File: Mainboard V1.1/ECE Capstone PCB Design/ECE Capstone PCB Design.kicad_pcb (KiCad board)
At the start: 2 copper layers, 81.9 x 68.9 mm, 71 parts, among them J1 1053131105, J2 1053131105, J3 Conn_01x40_Socket, J6 60S019P-301N-B1-FEC, U1 MCP2518FDT-H/SL, U2 MCP2542FD-E/SN, U5 TPS562201, U6 TPS61165DBV, U7 TPS562201

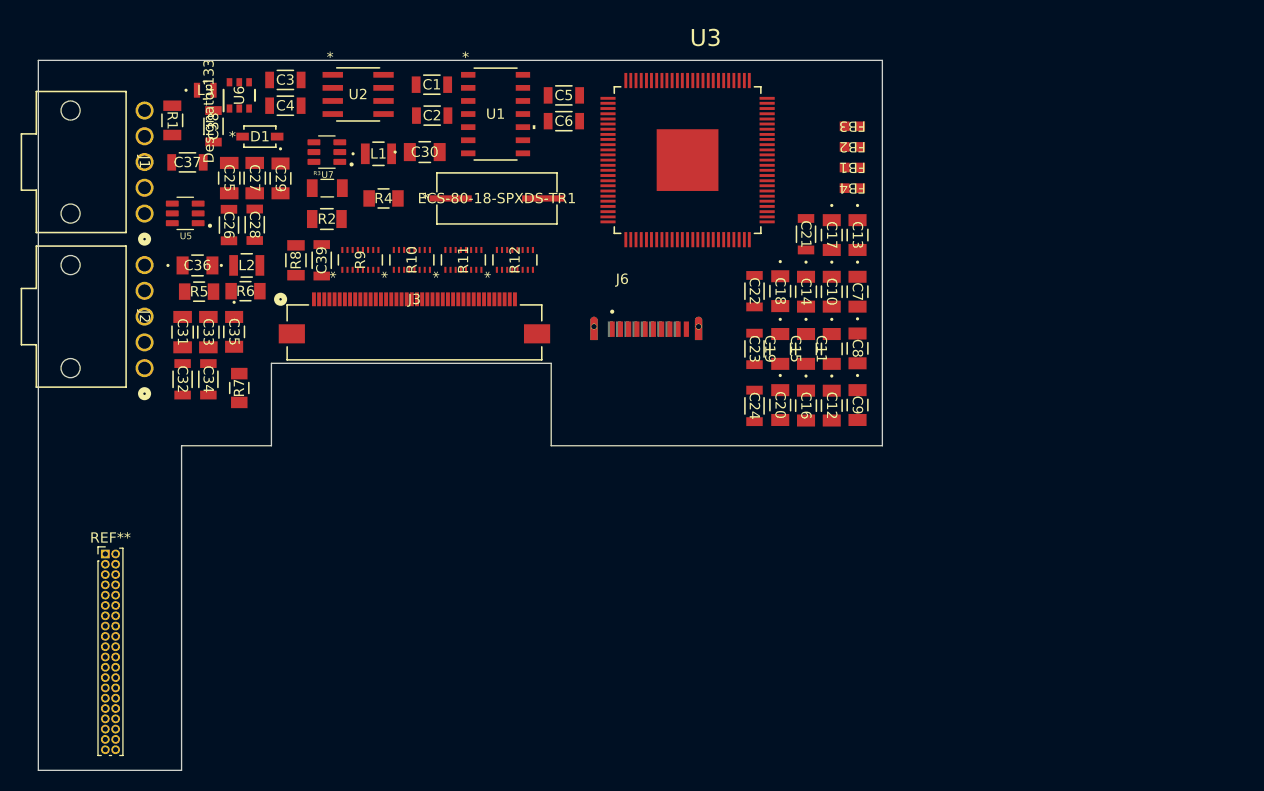
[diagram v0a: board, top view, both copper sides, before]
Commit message: Changed dev mode pin from 5V to 3.3V to comply with rasp pi high logic voltage. Changed some traces to remove any sharp angles and create more uniform lines where possible. Updated M2.5 screw cutouts to ensure they were accurate. Rounded the corners of the PCB to match that of the rasp pi. To do: Add 1mm of width to the bottom where the pi will be placed so that the pi lines up with the mainboard when placed. Move ferrite beads an appropriate distance away from the screw hole in the top right corner to maintain proper screw clearance.
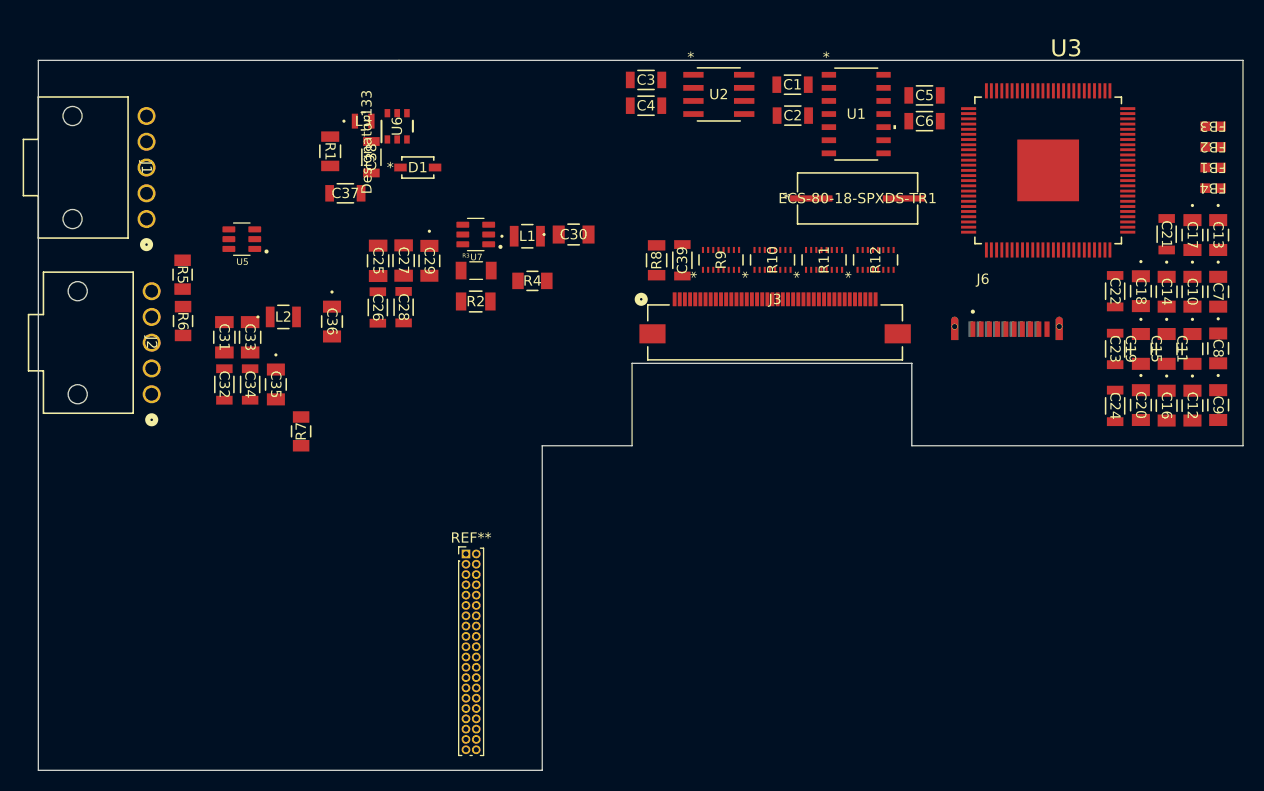
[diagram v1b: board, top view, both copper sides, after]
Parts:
- moved U3 35.0 mm to (202.0, 57.8)
- moved C1 35.0 mm to (177.2, 49.5)
- moved C10 35.0 mm to (216.0, 69.6)
- moved C11 35.0 mm to (216.0, 75.1)
- moved C12 35.0 mm to (216.0, 80.6)
- moved C13 35.0 mm to (218.5, 64.1)
- moved C14 35.0 mm to (213.5, 69.6)
- moved C15 35.0 mm to (213.5, 75.1)
- moved C16 35.0 mm to (213.5, 80.6)
- moved C17 35.0 mm to (216.0, 64.1)
- moved C18 35.0 mm to (211.0, 69.5)
- moved C19 35.0 mm to (211.0, 75.1)
- moved C2 35.0 mm to (177.2, 52.5)
- moved C20 35.0 mm to (211.0, 80.6)
- moved C21 35.0 mm to (213.5, 64.0)
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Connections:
- U5 pad 1: +3.3V -> /GND
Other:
- board size 81.9 x 68.9 mm -> 116.9 x 68.9 mm
